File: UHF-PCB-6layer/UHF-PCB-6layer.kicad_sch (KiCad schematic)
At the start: 26 parts, among them IC1 MC100EL1648DG, J1 Screw_Terminal_01x07, U1 MAC-24+, U2 LTC1566-1IS8-PBF, U3 TAV1-331+, U5 XMSM0G3507SPT, U6 XC7A100T-CSG324_A

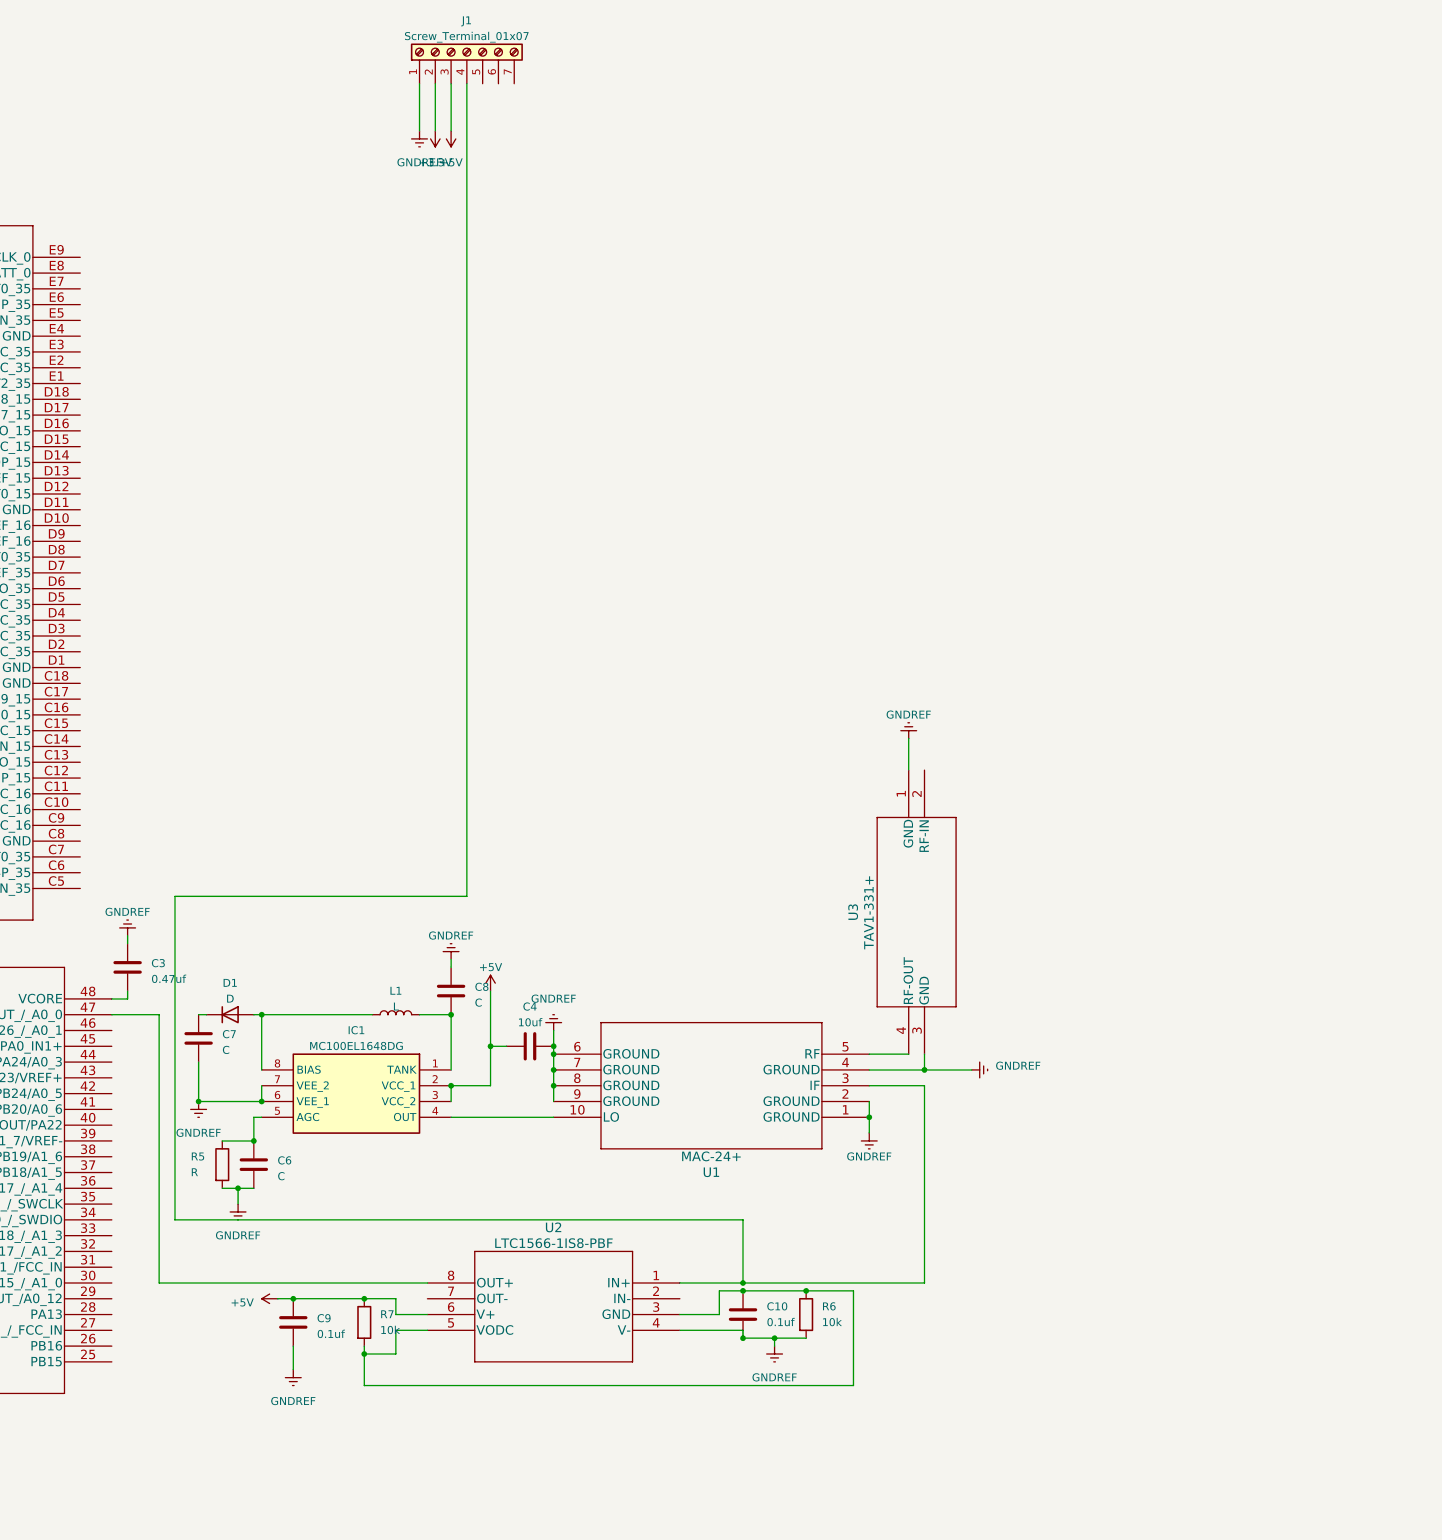
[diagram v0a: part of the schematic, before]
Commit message: added first part of tx side in schematic
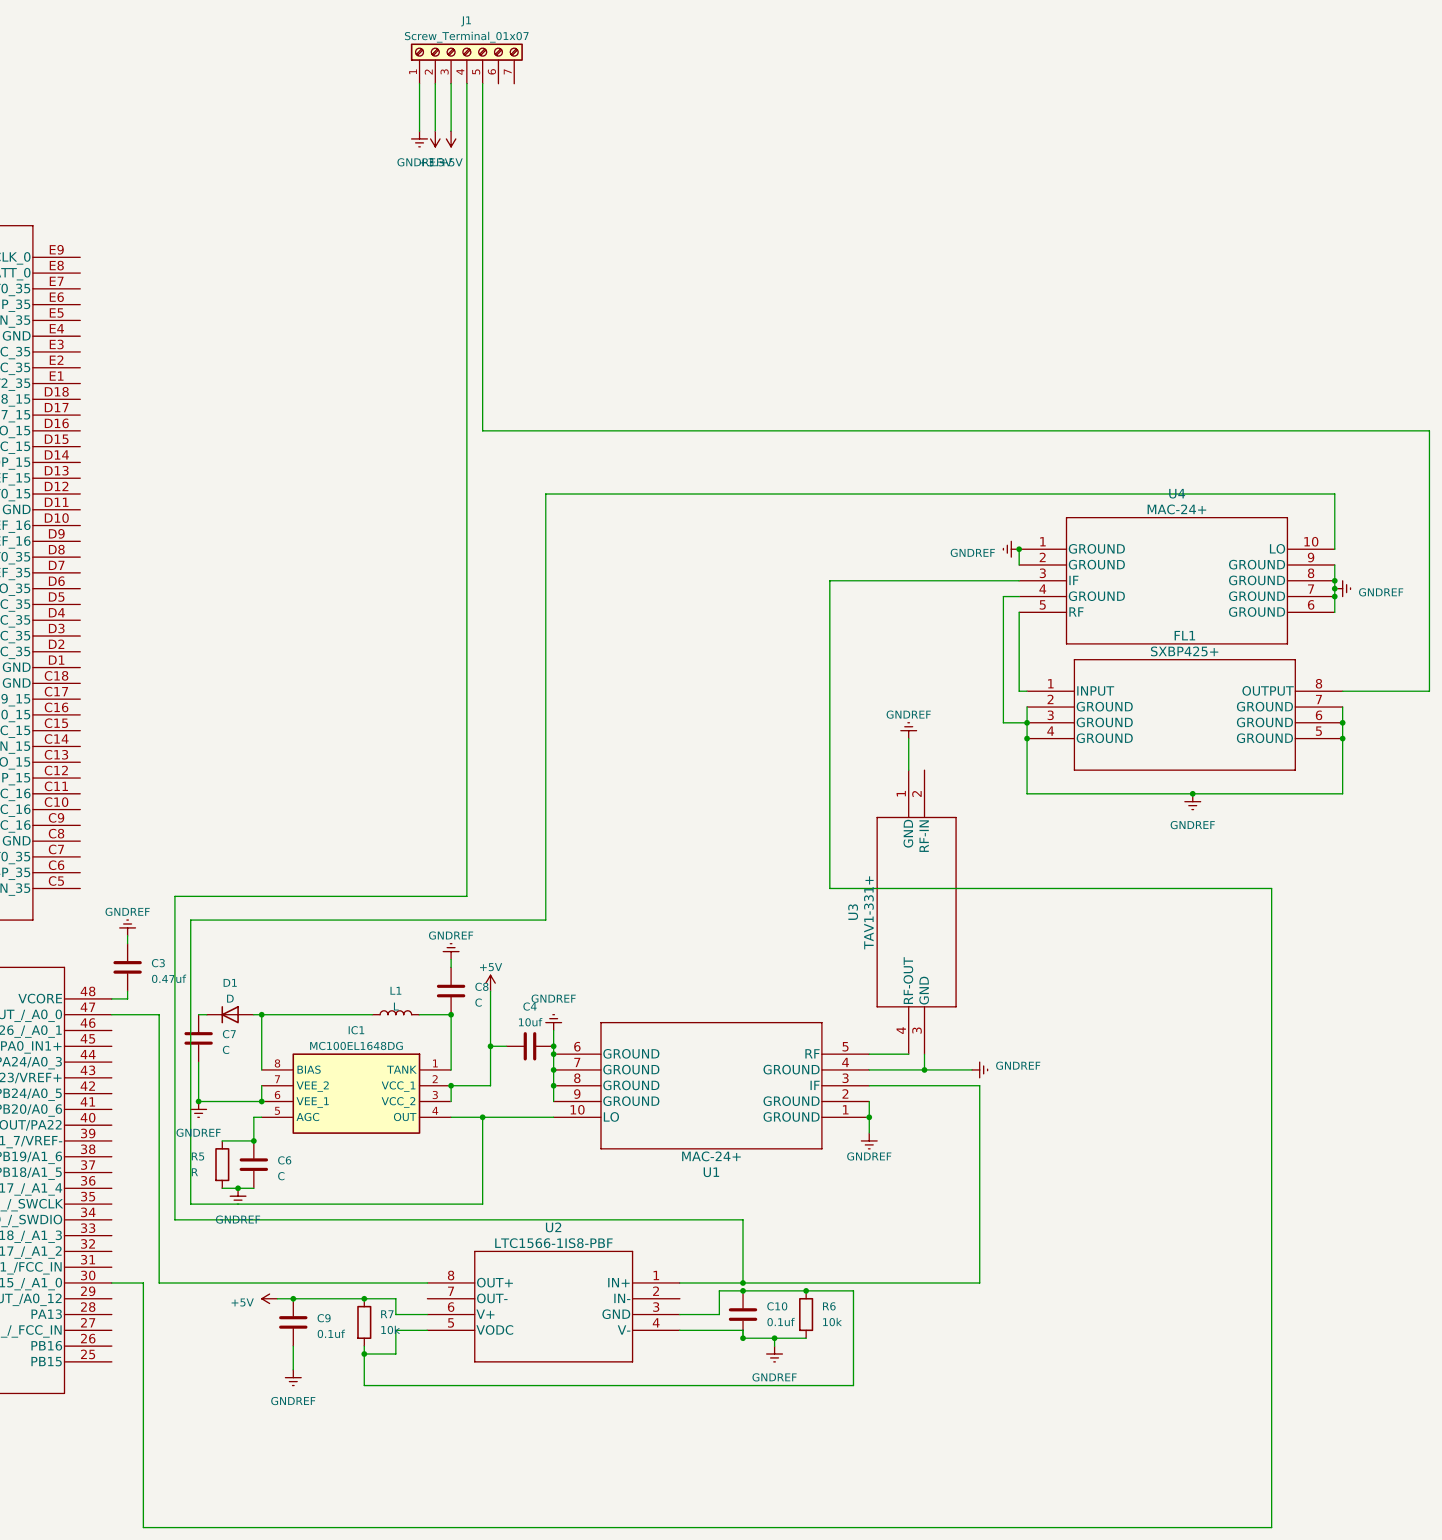
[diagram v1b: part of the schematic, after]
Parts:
- added FL1: SXBP425+, HF1139_MNC, symbol bandpass:SXBP425+
- added U4: MAC-24+, DZ1650_MNC, symbol 2023-12-20_00-32-43:MAC-24+
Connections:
- net GNDREF: now also FL1.2 (GROUND), FL1.3 (GROUND), FL1.4 (GROUND), FL1.5 (GROUND), FL1.6 (GROUND), FL1.7 (GROUND), U4.1 (GROUND), U4.2 (GROUND), U4.4 (GROUND), U4.6 (GROUND), U4.7 (GROUND), U4.8 (GROUND), U4.9 (GROUND)
- net at J1.5 (Pin_5): now also FL1.8 (OUTPUT)
- net at IC1.4 (OUT), U1.10 (LO): now also U4.10 (LO)
- net at U5.30 (PA15_/_A1_0): now also U4.3 (IF)
- new net: FL1.1 (INPUT), U4.5 (RF)

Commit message: added tx/rx from MC and working on FPGA
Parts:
- added J2: Screw_Terminal_01x04, TerminalBlock:TerminalBlock_bornier-4_P5.08mm, symbol Connector:Screw_Terminal_01x04
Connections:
- net +3.3V: now also U6.A17 (VCCO_15), U6.A7 (VCCO_35), U6.B10 (VCCO_16), U6.C13 (VCCO_15), U6.C3 (VCCO_35), U6.D16 (VCCO_15), U6.D6 (VCCO_35)
- net GNDREF: now also U6.A12 (GND), U6.A2 (GND), U6.B15 (GND), U6.B5 (GND), U6.C18 (GND), U6.C8 (GND), U6.D1 (GND), U6.D11 (GND), U6.E4 (GND)
- net at J1.6 (Pin_6): now also U3.2 (RF-IN)
- net at U2.8 (OUT+): now also U5.45 (PA25/A0_2/OPA0_IN1+); no longer U5.47 (PA27_/_RTC_OUT_/_A0_0)
- net at U5.40 (A0_7/CLK_OUT/PA22): now also J2.1 (Pin_1)
- net at U5.43 (PA23/VREF+): now also J2.2 (Pin_2)

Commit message: added LEDs and finished of the FPGA
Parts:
- added D2, D3, D4, D5: LED, LED_SMD:LED_2010_5025Metric_Pad1.52x2.65mm_HandSolder, symbol Device:LED
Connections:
- net GNDREF: now also D2.1 (K), D3.1 (K), D4.1 (K), D5.1 (K)
- net at J2.1 (Pin_1), U5.40 (A0_7/CLK_OUT/PA22): now also D4.2 (A)
- net at J2.2 (Pin_2), U5.43 (PA23/VREF+): now also D5.2 (A)
- net at U6.B16 (IO_L7P_T1_AD2P_15): now also J2.4 (Pin_4), D3.2 (A)
- net at U6.B17 (IO_L7N_T1_AD2N_15): now also J2.3 (Pin_3), D2.2 (A)
- net +1V0: now reaches U6.E8 (VCCBATT_0)

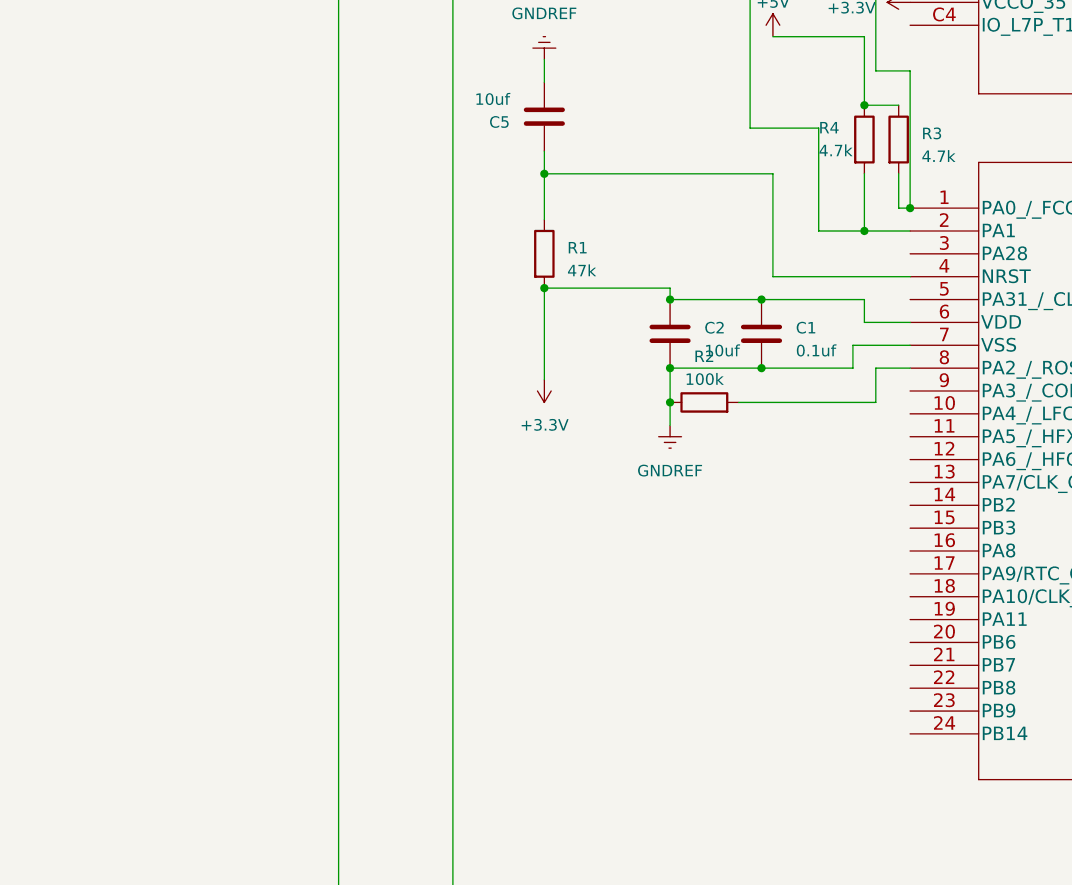
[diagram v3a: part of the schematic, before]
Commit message: wdt draft added
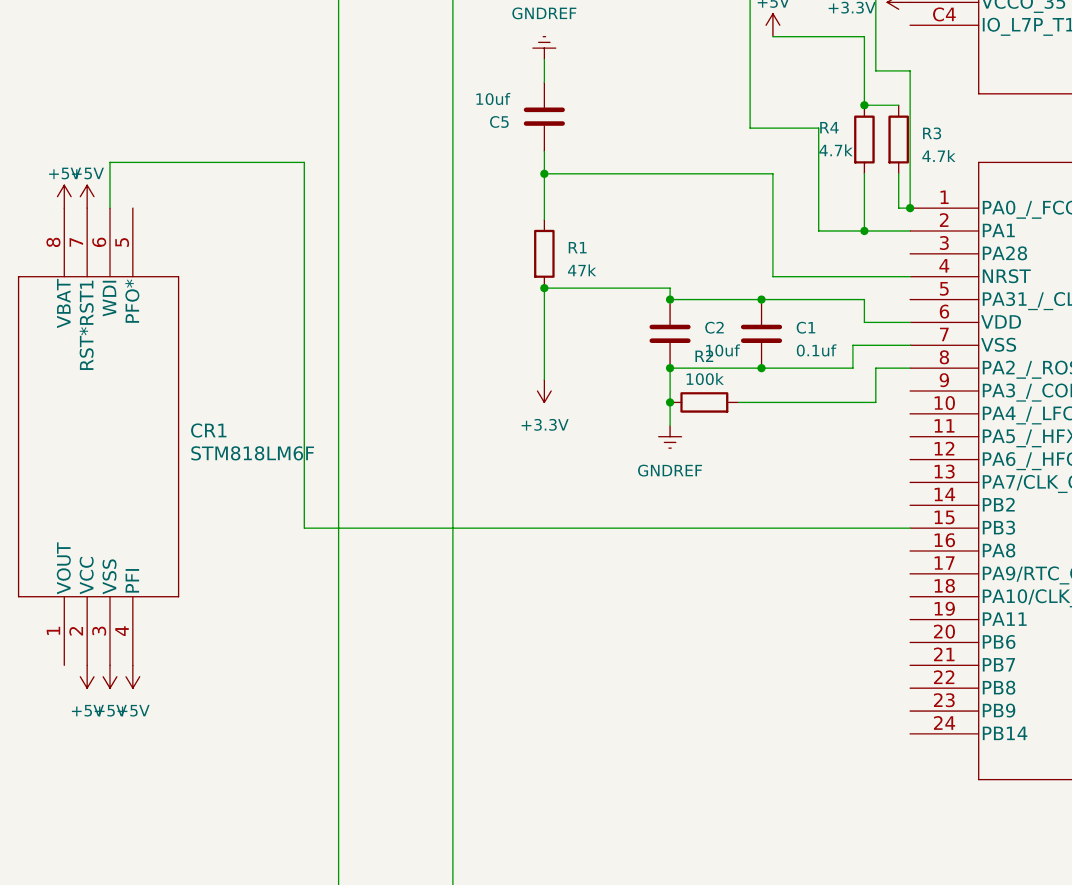
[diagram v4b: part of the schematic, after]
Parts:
- added CR1: STM818LM6F, SO-8_STM, symbol WDT:STM818LM6F
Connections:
- net +5V: now also CR1.2 (VCC), CR1.3 (VSS), CR1.4 (PFI), CR1.7 (RST*RST1), CR1.8 (VBAT)
- net at U5.15 (PB3): now also CR1.6 (WDI)
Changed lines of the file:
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@@
+    (stroke (width 0) (type default))
+  )
+  (wire (pts (xy 39.37 166.37) (xy 39.37 171.45))
     (stroke (width 0) (type default))
   )
@@
     (stroke (width 0) (type default))
   )
+  (wire (pts (xy 60.96 166.37) (xy 39.37 166.37))
+    (stroke (width 0) (type default))
+  )
   (wire (pts (xy 337.82 27.94) (xy 342.9 27.94))
     (stroke (width 0) (type default))
@@
     (stroke (width 0) (type default))
   )
+  (wire (pts (xy 128.27 207.01) (xy 60.96 207.01))
+    (stroke (width 0) (type default))
+  )
   (wire (pts (xy 101.6 181.61) (xy 111.76 181.61))
     (stroke (width 0) (type default))
@@
     (stroke (width 0) (type default))
   )
+  (wire (pts (xy 60.96 207.01) (xy 60.96 166.37))
+    (stroke (width 0) (type default))
+  )
   (wire (pts (xy 128.27 171.45) (xy 127 171.45))
     (stroke (width 0) (type default))
@@
         (path "/408f5dbf-8c57-4b84-b0cc-1d788fcf6d08"
           (reference "L1") (unit 1)
+        )
+      )
+    )
+  )
+  (symbol (lib_id "power:+5V") (at 34.29 171.45 0) (unit 1)
+    (in_bom yes) (on_board yes) (dnp no) (fields_autoplaced)
+    (property "Reference" "#PWR045" (at 34.29 175.26 0)
+      (effects (font (size 1.27 1.27)) hide)
+    )
+    (property "Value" "+5V" (at 34.29 167.64 0)
+      (effects (font (size 1.27 1.27)))
+    )
+    (property "Footprint" "" (at 34.29 171.45 0)
+      (effects (font (size 1.27 1.27)) hide)
+    )
+    (property "Datasheet" "" (at 34.29 171.45 0)
+      (effects (font (size 1.27 1.27)) hide)
+    )
+    (pin "1")
+    (instances
+      (project "UHF-PCB-6layer"
+        (path "/408f5dbf-8c57-4b84-b0cc-1d788fcf6d08"
+          (reference "#PWR045") (unit 1)
         )
       )
@@
         (path "/408f5dbf-8c57-4b84-b0cc-1d788fcf6d08"
           (reference "#PWR027") (unit 1)
+        )
+      )
+    )
+  )
+  (symbol (lib_id "WDT:STM818LM6F") (at 34.29 222.25 90) (unit 1)
+    (in_bom yes) (on_board yes) (dnp no) (fields_autoplaced)
+    (property "Reference" "CR1" (at 48.26 196.215 90)
+      (effects (font (size 1.524 1.524)) (justify right))
+    )
+    (property "Value" "STM818LM6F" (at 48.26 198.755 90)
+      (effects (font (size 1.524 1.524)) (justify right))
+    )
+    (property "Footprint" "SO-8_STM" (at 28.194 196.85 0)
+      (effects (font (size 1.524 1.524)) hide)
+    )
+    (property "Datasheet" "" (at 34.29 222.25 0)
+      (effects (font (size 1.524 1.524)))
+    )
+    (pin "1")
+    (pin "2")
+    (pin "3")
+    (pin "4")
+    (pin "5")
+    (pin "6")
+    (pin "7")
+    (pin "8")
+    (instances
+      (project "UHF-PCB-6layer"
+        (path "/408f5dbf-8c57-4b84-b0cc-1d788fcf6d08"
+          (reference "CR1") (unit 1)
         )
       )
@@
     )
   )
+  (symbol (lib_id "power:+5V") (at 36.83 222.25 180) (unit 1)
+    (in_bom yes) (on_board yes) (dnp no) (fields_autoplaced)
+    (property "Reference" "#PWR043" (at 36.83 218.44 0)
+      (effects (font (size 1.27 1.27)) hide)
+    )
+    (property "Value" "+5V" (at 36.83 227.33 0)
+      (effects (font (size 1.27 1.27)))
+    )
+    (property "Footprint" "" (at 36.83 222.25 0)
+      (effects (font (size 1.27 1.27)) hide)
+    )
+    (property "Datasheet" "" (at 36.83 222.25 0)
+      (effects (font (size 1.27 1.27)) hide)
+    )
+    (pin "1")
+    (instances
+      (project "UHF-PCB-6layer"
+        (path "/408f5dbf-8c57-4b84-b0cc-1d788fcf6d08"
+          (reference "#PWR043") (unit 1)
+        )
+      )
+    )
+  )
   (symbol (lib_id "power:+3.3V") (at 240.03 80.01 270) (unit 1)
     (in_bom yes) (on_board yes) (dnp no) (fields_autoplaced)
@@
         (path "/408f5dbf-8c57-4b84-b0cc-1d788fcf6d08"
           (reference "#PWR035") (unit 1)
+        )
+      )
+    )
+  )
+  (symbol (lib_id "power:+5V") (at 39.37 222.25 180) (unit 1)
+    (in_bom yes) (on_board yes) (dnp no) (fields_autoplaced)
+    (property "Reference" "#PWR044" (at 39.37 218.44 0)
+      (effects (font (size 1.27 1.27)) hide)
+    )
+    (property "Value" "+5V" (at 39.37 227.33 0)
+      (effects (font (size 1.27 1.27)))
+    )
+    (property "Footprint" "" (at 39.37 222.25 0)
+      (effects (font (size 1.27 1.27)) hide)
+    )
+    (property "Datasheet" "" (at 39.37 222.25 0)
+      (effects (font (size 1.27 1.27)) hide)
+    )
+    (pin "1")
+    (instances
+      (project "UHF-PCB-6layer"
+        (path "/408f5dbf-8c57-4b84-b0cc-1d788fcf6d08"
+          (reference "#PWR044") (unit 1)
         )
       )
@@
     )
   )
+  (symbol (lib_id "power:+5V") (at 41.91 222.25 180) (unit 1)
+    (in_bom yes) (on_board yes) (dnp no) (fields_autoplaced)
+    (property "Reference" "#PWR046" (at 41.91 218.44 0)
+      (effects (font (size 1.27 1.27)) hide)
+    )
+    (property "Value" "+5V" (at 41.91 227.33 0)
+      (effects (font (size 1.27 1.27)))
+    )
+    (property "Footprint" "" (at 41.91 222.25 0)
+      (effects (font (size 1.27 1.27)) hide)
+    )
+    (property "Datasheet" "" (at 41.91 222.25 0)
+      (effects (font (size 1.27 1.27)) hide)
+    )
+    (pin "1")
+    (instances
+      (project "UHF-PCB-6layer"
+        (path "/408f5dbf-8c57-4b84-b0cc-1d788fcf6d08"
+          (reference "#PWR046") (unit 1)
+        )
+      )
+    )
+  )
   (symbol (lib_id "power:GNDREF") (at 294.64 31.75 0) (unit 1)
     (in_bom yes) (on_board yes) (dnp no) (fields_autoplaced)
@@
         )
       )
+    )
+  )
+  (symbol (lib_id "power:+5V") (at 36.83 171.45 0) (unit 1)
+    (in_bom yes) (on_board yes) (dnp no) (fields_autoplaced)
+    (property "Reference" "#PWR047" (at 36.83 175.26 0)
+      (effects (font (size 1.27 1.27)) hide)
+    )
+    (property "Value" "+5V" (at 36.83 167.64 0)
+      (effects (font (size 1.27 1.27)))
+    )
+    (property "Footprint" "" (at 36.83 171.45 0)
+      (effects (font (size 1.27 1.27)) hide)
+    )
+    (property "Datasheet" "" (at 36.83 171.45 0)
+      (effects (font (size 1.27 1.27)) hide)
+    )
+    (pin "1")
+    (instances
+      (project "UHF-PCB-6layer"
+        (path "/408f5dbf-8c57-4b84-b0cc-1d788fcf6d08"
+          (reference "#PWR047") (unit 1)
+        )
+      )
